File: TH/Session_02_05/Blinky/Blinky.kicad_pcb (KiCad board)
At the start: 2 copper layers, 38.1 x 38.1 mm, 12 parts, among them U1 TLC551CD‎

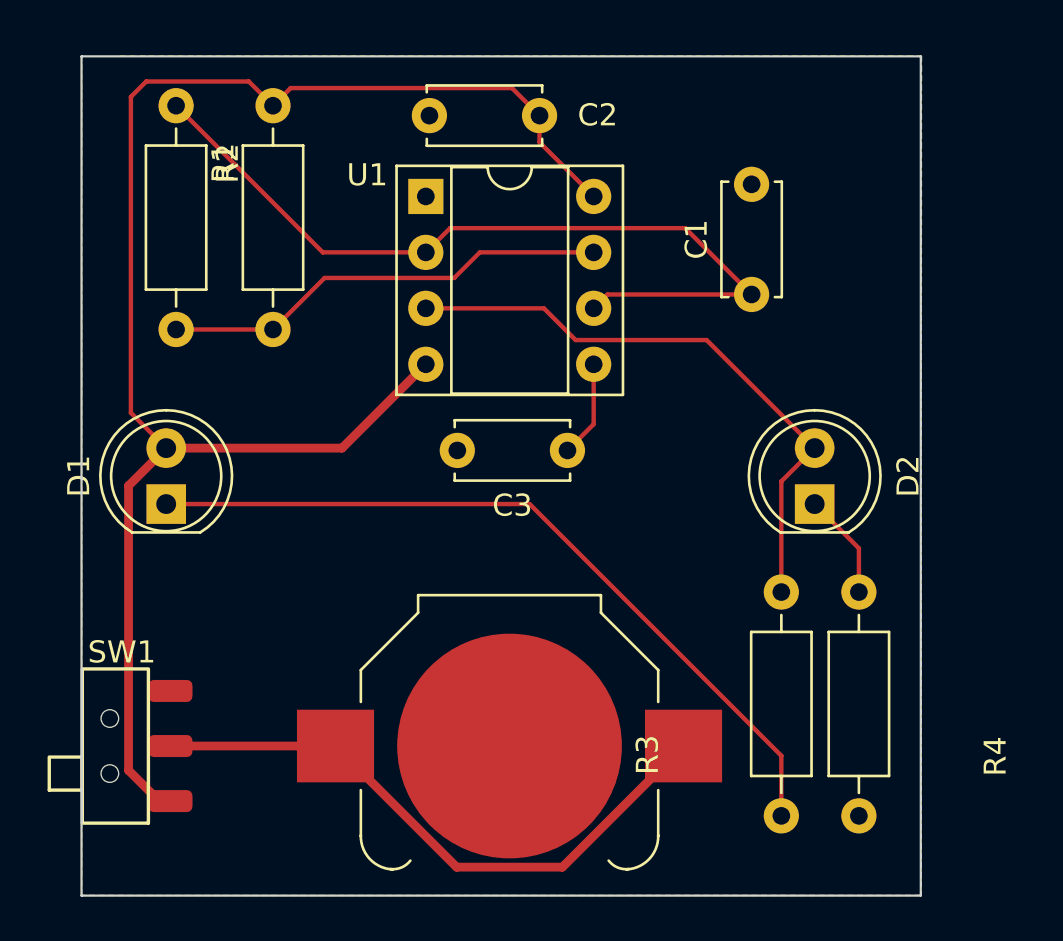
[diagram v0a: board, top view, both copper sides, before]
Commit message: Revamps the through-hole project as transistor based
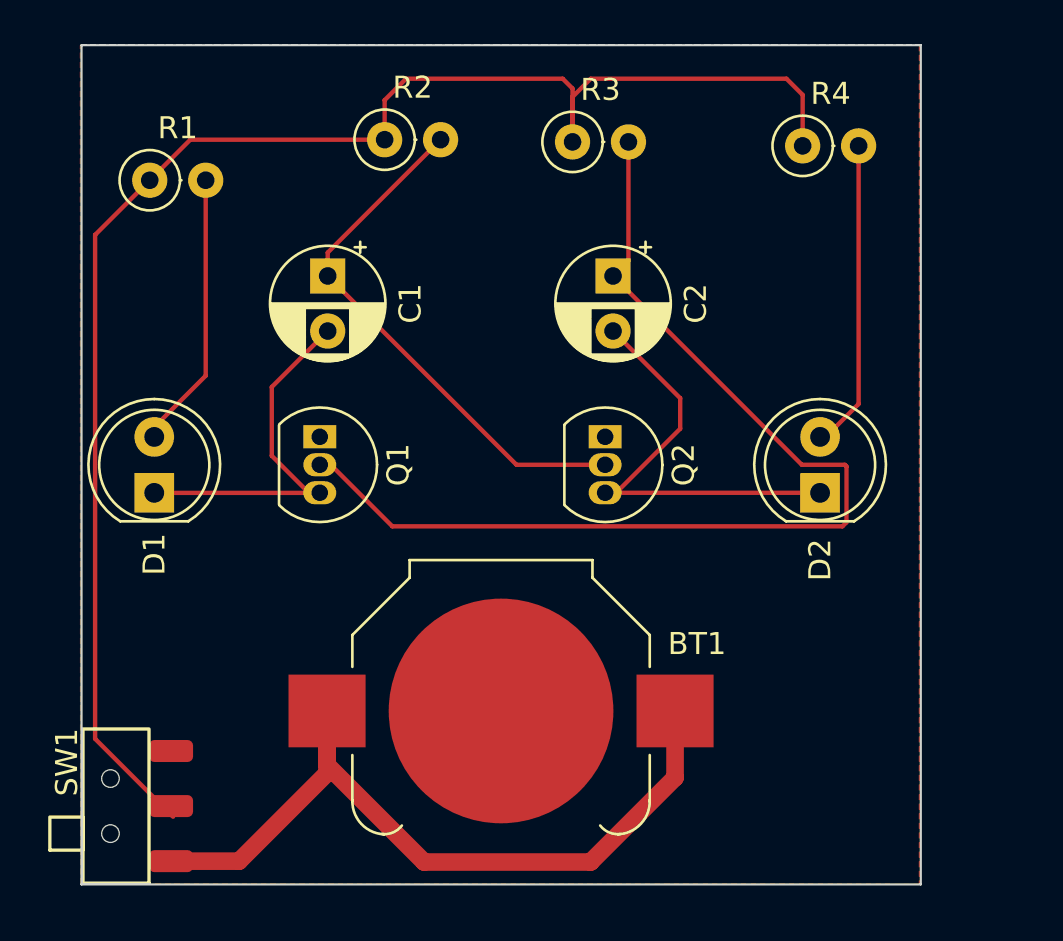
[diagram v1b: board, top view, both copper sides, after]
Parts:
- removed C3: 100nF, Capacitor_THT:C_Disc_D5.0mm_W2.5mm_P5.00mm
- removed SW?: SW_SPDT, Blinky_ZAM:SSK-1202
- removed U1: TLC551CD‎, Package_DIP:DIP-8_W7.62mm_Socket
- added Q1: 2N3904, Package_TO_SOT_THT:TO-92_Inline, F.Cu at (137.8, 93.5)
- added Q2: 2N3904, Package_TO_SOT_THT:TO-92_Inline, F.Cu at (150.8, 93.5)
- added SW1: SW_SPST, Blinky_ZAM:SSK-1202, F.Cu at (131.1, 110.2)
- C1: value 300nF -> 10μF; footprint Capacitor_THT:C_Disc_D5.0mm_W2.5mm_P5.00mm -> Capacitor_THT:CP_Radial_D5.0mm_P2.50mm
- C2: value 100nF -> 10μF; footprint Capacitor_THT:C_Disc_D5.0mm_W2.5mm_P5.00mm -> Capacitor_THT:CP_Radial_D5.0mm_P2.50mm
- R1: value 10kΩ -> 220Ω; footprint Resistor_THT:R_Axial_DIN0207_L6.3mm_D2.5mm_P10.16mm_Horizontal -> Resistor_THT:R_Axial_DIN0207_L6.3mm_D2.5mm_P2.54mm_Vertical
- R2: value 1MΩ -> 100kΩ; footprint Resistor_THT:R_Axial_DIN0207_L6.3mm_D2.5mm_P10.16mm_Horizontal -> Resistor_THT:R_Axial_DIN0207_L6.3mm_D2.5mm_P2.54mm_Vertical
- R3: value 200Ω -> 100kΩ; footprint Resistor_THT:R_Axial_DIN0207_L6.3mm_D2.5mm_P10.16mm_Horizontal -> Resistor_THT:R_Axial_DIN0207_L6.3mm_D2.5mm_P2.54mm_Vertical
- R4: value 200Ω -> 220Ω; footprint Resistor_THT:R_Axial_DIN0207_L6.3mm_D2.5mm_P10.16mm_Horizontal -> Resistor_THT:R_Axial_DIN0207_L6.3mm_D2.5mm_P2.54mm_Vertical
- moved R3 32.0 mm to (149.3, 80.1), turned to 0 degrees
- moved R4 20.4 mm to (159.7, 80.3), turned to 0 degrees
- moved C1 19.3 mm to (138.2, 86.2), turned to -90 degrees
- moved R2 12.8 mm to (140.8, 80.0), turned to 0 degrees
- moved C2 8.01 mm to (151.1, 86.2), turned to -90 degrees
- moved R1 6.54 mm to (130.1, 81.8), turned to 0 degrees
- moved BT1 1.64 mm to (146.0, 105.9)
- moved D1 0.74 mm to (130.3, 96.0)
- moved D2 0.56 mm to (160.5, 96.0)
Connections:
- C1 pad 2: GND -> Net-(C1-Pad2)
- C2 pad 2: GND -> Net-(C2-Pad2)
- D1 pad 1: Net-(D1-Pad1) -> Net-(C1-Pad2)
- D1 pad 2: Net-(C2-Pad1) -> Net-(D1-Pad2)
- D2 pad 1: Net-(D2-Pad1) -> Net-(C2-Pad2)
- R1 pad 1: Net-(C2-Pad1) -> Net-(R1-Pad1)
- R1 pad 2: Net-(R1-Pad2) -> Net-(D1-Pad2)
- R2 pad 1: Net-(R1-Pad2) -> Net-(R1-Pad1)
- R3 pad 1: Net-(D1-Pad1) -> Net-(R1-Pad1)
- R3 pad 2: Net-(D2-Pad2) -> Net-(C2-Pad1)
- R4 pad 1: Net-(D2-Pad1) -> Net-(R1-Pad1)
- R4 pad 2: GND -> Net-(D2-Pad2)
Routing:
- net Net-(R1-Pad1): track 0.00 -> 71.6 mm
- net Net-(D1-Pad1): track 35.4 -> 0.00 mm
- net Net-(C2-Pad1): track 72.6 -> 48.2 mm
- net Net-(R1-Pad2): track 20.4 -> 0.00 mm
- net Net-(C2-Pad2): track 0.00 -> 20.1 mm
- net Net-(C1-Pad2): track 0.00 -> 17.1 mm
- net Net-(C1-Pad1): track 38.0 -> 24.5 mm
- net Net-(D2-Pad2): track 27.4 -> 14.2 mm
- net Net-(D1-Pad2): track 0.00 -> 13.2 mm
- net Net-(BT1-Pad1): track 27.9 -> 36.3 mm
- net Net-(D2-Pad1): track 4.83 -> 0.00 mm
- net Net-(C3-Pad1): track 4.40 -> 0.00 mm
- removed copper zone on B.Cu, net GND

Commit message: Makes corrections to the design rules
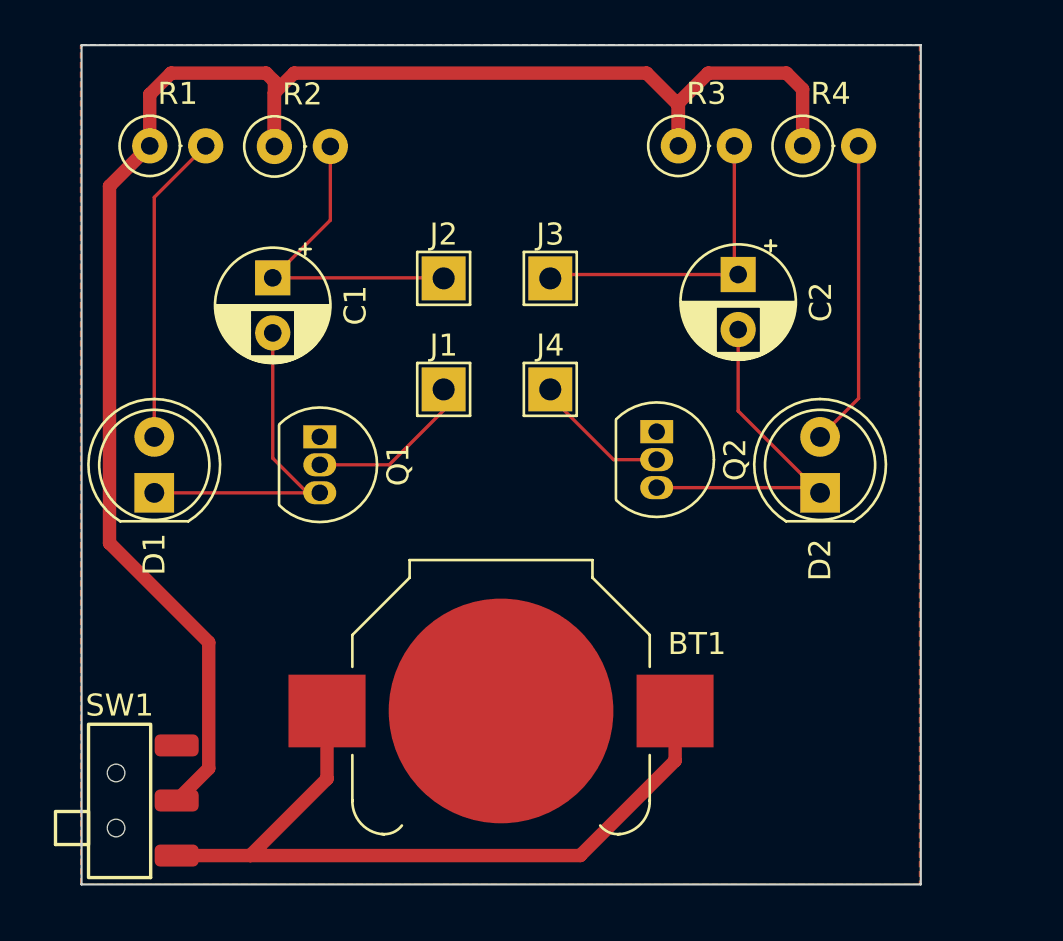
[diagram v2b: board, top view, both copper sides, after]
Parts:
- added J1: Jumper_1, TestPoint:TestPoint_THTPad_2.0x2.0mm_Drill1.0mm, F.Cu at (143.4, 91.3)
- added J2: Jumper_1, TestPoint:TestPoint_THTPad_2.0x2.0mm_Drill1.0mm, F.Cu at (143.4, 86.3)
- added J4: Jumper_1, TestPoint:TestPoint_THTPad_2.0x2.0mm_Drill1.0mm, F.Cu at (148.3, 91.3)
- added J?: Jumper_1, TestPoint:TestPoint_THTPad_2.0x2.0mm_Drill1.0mm, F.Cu at (148.3, 86.3)
- moved C2 5.68 mm to (156.8, 86.1)
- moved R2 5.01 mm to (135.8, 80.3)
- moved R3 4.81 mm to (154.1, 80.3)
- moved C1 2.50 mm to (135.7, 86.3)
- moved Q2 2.35 mm to (153.1, 93.2)
- moved R1 1.56 mm to (130.1, 80.3)
- moved SW1 0.36 mm to (131.3, 110.0)
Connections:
- Q1 pad 2: Net-(C2-Pad1) -> Net-(J1-Pad1)
- Q2 pad 2: Net-(C1-Pad1) -> Net-(J4-Pad1)
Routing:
- net Net-(C2-Pad1): track 48.2 -> 14.5 mm
- net Net-(C1-Pad1): track 24.5 -> 14.8 mm
- net Net-(J1-Pad1): track 0.00 -> 7.60 mm
- net Net-(R1-Pad1): track 71.6 -> 79.1 mm
- net Net-(J4-Pad1): track 0.00 -> 6.34 mm
- net Net-(C2-Pad2): track 20.1 -> 16.5 mm
- net Net-(BT1-Pad1): track 36.3 -> 34.7 mm
- net Net-(C1-Pad2): track 17.1 -> 16.0 mm
- net Net-(D1-Pad2): track 13.2 -> 14.2 mm

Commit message: Corrections to the switch footprint
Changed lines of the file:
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@@
       (effects (font (size 1 1) (thickness 0.15)))
     )
+    (fp_rect (start -3.500001 -1.1) (end 3.500001 -4) (layer "F.SilkS") (width 0.1524) (fill none))
     (fp_rect (start -2 -5.499999) (end -0.5 -4) (layer "F.SilkS") (width 0.1524) (fill none))
-    (fp_rect (start -3.500001 -1.18) (end 3.46 -4) (layer "F.SilkS") (width 0.1524) (fill none))
     (fp_rect (start -3.5 -5.5) (end 3.5 1) (layer "F.CrtYd") (width 0.01) (fill none))
-    (pad "" np_thru_hole circle (at 1.25 -2.75 90) (size 0.8 0.8) (drill 0.8) (layers F&B.Cu *.Mask))
-    (pad "" np_thru_hole circle (at -1.25 -2.75 90) (size 0.8 0.8) (drill 0.8) (layers F&B.Cu *.Mask))
+    (pad "" np_thru_hole circle (at 1.5 -2.75 90) (size 0.8 0.8) (drill 0.8) (layers F&B.Cu *.Mask))
+    (pad "" np_thru_hole circle (at -1.5 -2.75 90) (size 0.8 0.8) (drill 0.8) (layers F&B.Cu *.Mask))
     (pad "1" smd roundrect (at -2.5 0 90) (size 1 2) (layers "F.Cu" "F.Paste" "F.Mask") (roundrect_rratio 0.25)
       (net 1 "Net-(BT1-Pad1)") (pinfunction "A") (pintype "passive"))
